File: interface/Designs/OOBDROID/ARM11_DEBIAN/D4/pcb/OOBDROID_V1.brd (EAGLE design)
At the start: 60.3 x 36.4 mm, 37 parts, among them T1 BC847, T2 BC817, U1 MCP2551, U2 MCP2551, X1 16MHz, X2 ODROID P1, X3 16MHz, X4 ODROID-P5

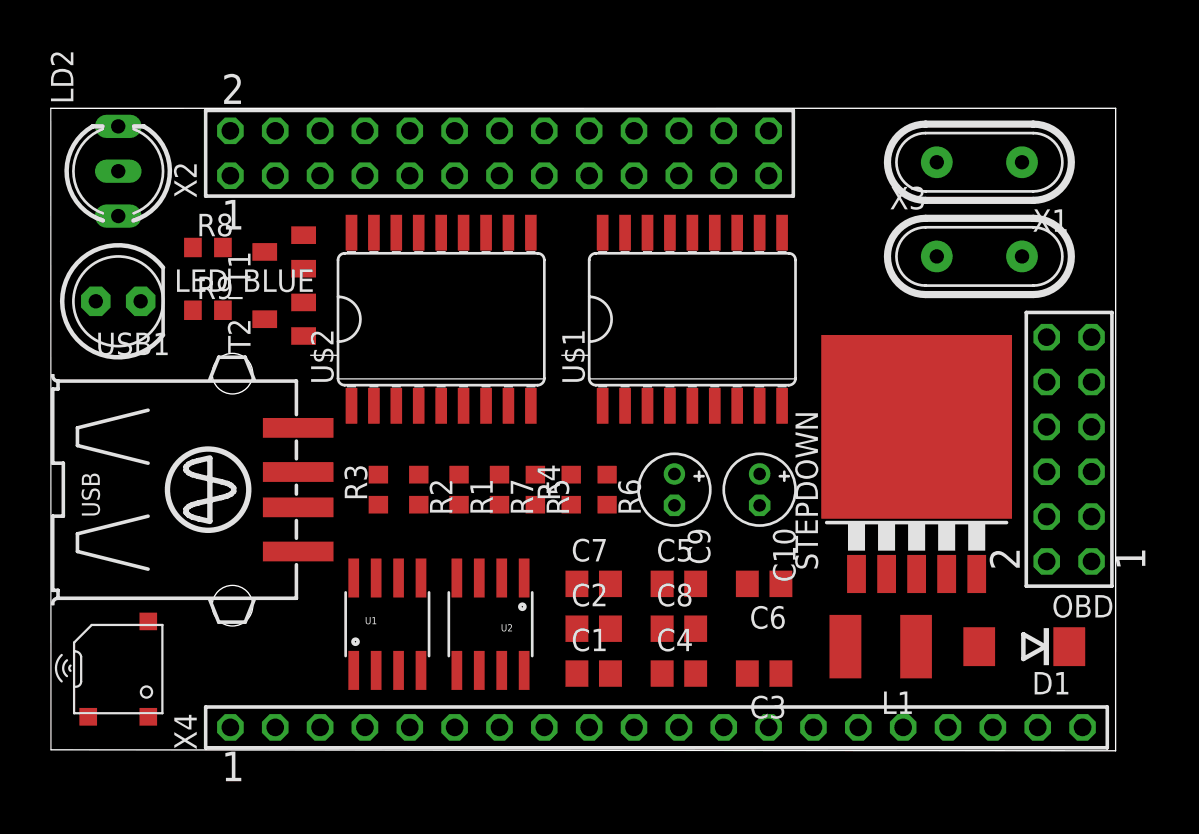
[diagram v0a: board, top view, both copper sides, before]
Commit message: add latest PCB/schematics modification for OOBDROID extension
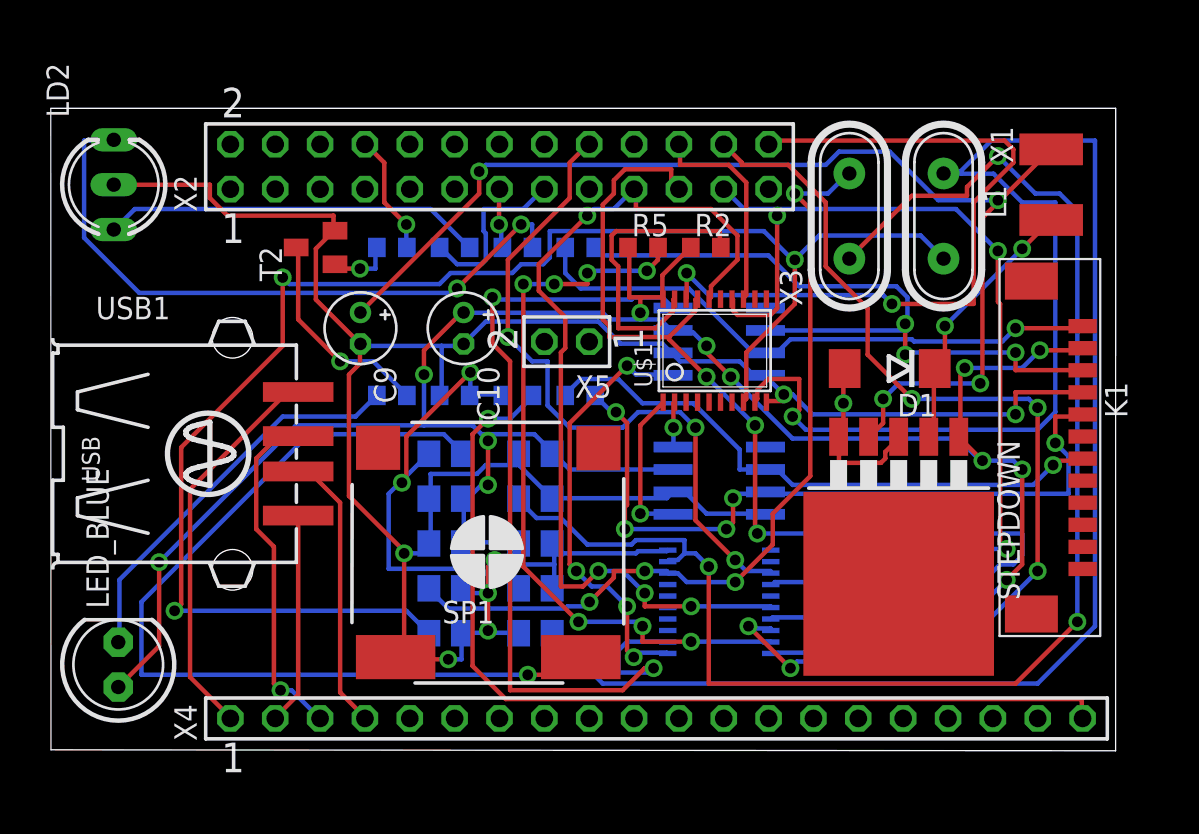
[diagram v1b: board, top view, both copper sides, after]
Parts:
- removed OBD: OOBD-CON, con-samtec:SSW-106-02-S-D
- removed R4: 4k7, eagle-ltspice:R0603
- removed SPK1: SMT-0540-S-R, adafruit:SMT-0540-S-R
- removed T1: BC847, transistor:SOT23
- added C11: 33nF, eagle-ltspice:C0805
- added C12: 10µF, eagle-ltspice:C0805
- added K1: OBD, EagleLibrary_Wuerth_Elektronik _eiCan_Wire_to_Board_Connectors_v6_20150113:653112124022
- added R12, R13: 150R, eagle-ltspice:R0603
- added SP1: LSF-15SMD, speaker:SMS-1308MS-2-R
- added X5: SSW-101-02-S-D, con-samtec:SSW-101-02-S-D
- U$1, U$2: value MCP2515SO -> MCP2515TSOP; device MCP2515_MT:SO18L -> MCP2515_MT:TSSOP20
- moved L1 27.9 mm to (56.6, 32.0), turned to 90 degrees
- moved U$2 22.5 mm to (37.8, 8.38), flipped to the bottom, turned to 90 degrees
- moved R2 21.3 mm to (37.1, 28.4), turned to 0 degrees
- moved U2 20.6 mm to (37.8, 23.1), flipped to the bottom, turned to 90 degrees
- moved LED_BLUE 20.6 mm to (3.81, 4.83), turned to 90 degrees
- moved U1 20.5 mm to (37.8, 15.2), flipped to the bottom, turned to 90 degrees
- moved C9 20.0 mm to (17.5, 23.9)
- moved C10 19.1 mm to (23.4, 23.9)
- moved R3 17.9 mm to (30.0, 28.4), flipped to the bottom, turned to 180 degrees
- moved D1 17.5 mm to (47.5, 21.6)
- moved R5 15.0 mm to (33.5, 28.4), turned to 0 degrees
- moved R6 14.6 mm to (26.4, 28.4), flipped to the bottom, turned to 180 degrees
- moved R7 13.9 mm to (22.9, 28.4), flipped to the bottom, turned to 0 degrees
- moved C4 13.4 mm to (22.4, 6.60), flipped to the bottom
- moved C5 13.4 mm to (22.4, 11.7), flipped to the bottom
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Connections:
- removed net N$20: SPK1.+, T1.3
- removed net N$21: R4.2, T1.1
- new net N$17: C12.2, SP1.M1
- new net N$37: C11.2, C12.1, R12.2, R13.2
- net GND: now also C11.1, K1.4, R13.1, SP1.M2, U$1.10, U$2.10; no longer OBD.4, T1.2, U$1.9, U$2.9
- net N$1: now also K1.5; no longer OBD.5
- net N$10: now also K1.1; no longer OBD.1
- net N$11: now also U$1.8; no longer U$1.7
- net N$12: now also U$1.9; no longer U$1.8
- net N$13: now also U$1.19; no longer U$1.17
- net N$16: now also K1.7; no longer OBD.7
- net N$19: now also U$1.18; no longer U$1.16
- net N$3: now also U$2.8; no longer U$2.7
- net N$30: now also R12.1, X4.20; no longer R4.1, X2.11
- net N$31: now also U$1.13; no longer U$1.12
- net N$32: now also U$2.13; no longer U$2.12
- net N$33: now also U$2.18; no longer U$2.16
- net N$38: now also U$1.16, U$2.16; no longer U$1.14, U$2.14
- net N$43: now also U$1.17, U$2.17; no longer U$1.15, U$2.15
- net N$44: now also U$1.14, U$2.14; no longer U$1.13, U$2.13
- net N$5: now also U$2.9; no longer U$2.8
- net N$6: now also U$2.19; no longer U$2.17
- net N$9: now also K1.3; no longer OBD.3
- net VCC: now also K1.2, U$1.20, U$2.20; no longer OBD.2, SPK1.-, U$1.18, U$2.18
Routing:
- net GND: track 0.00 -> 156.7 mm, vias 0 -> 8
- net VCC: track 0.00 -> 139.4 mm, vias 0 -> 12
- net N$12: track 0.00 -> 109.4 mm, vias 0 -> 1
- net N$11: track 0.00 -> 87.1 mm, vias 0 -> 3
- net N$5: track 0.00 -> 83.3 mm, vias 0 -> 3
- net N$43: track 0.00 -> 65.5 mm, vias 0 -> 3
- net N$4: track 0.00 -> 65.1 mm, vias 0 -> 4
- net N$33: track 0.00 -> 58.0 mm, vias 0 -> 5
- net N$44: track 0.00 -> 57.3 mm, vias 0 -> 3
- net N$30: track 0.00 -> 53.8 mm, vias 0 -> 1
- net N$17: track 0.00 -> 52.6 mm, vias 0 -> 1
- net N$38: track 0.00 -> 51.6 mm, vias 0 -> 4
- net N$7: track 0.00 -> 48.3 mm, vias 0 -> 2
- net N$3: track 0.00 -> 46.9 mm, vias 0 -> 4
- net N$19: track 0.00 -> 42.4 mm, vias 0 -> 2
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
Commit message: add latest modifcation of OOBDROID to new feature branch
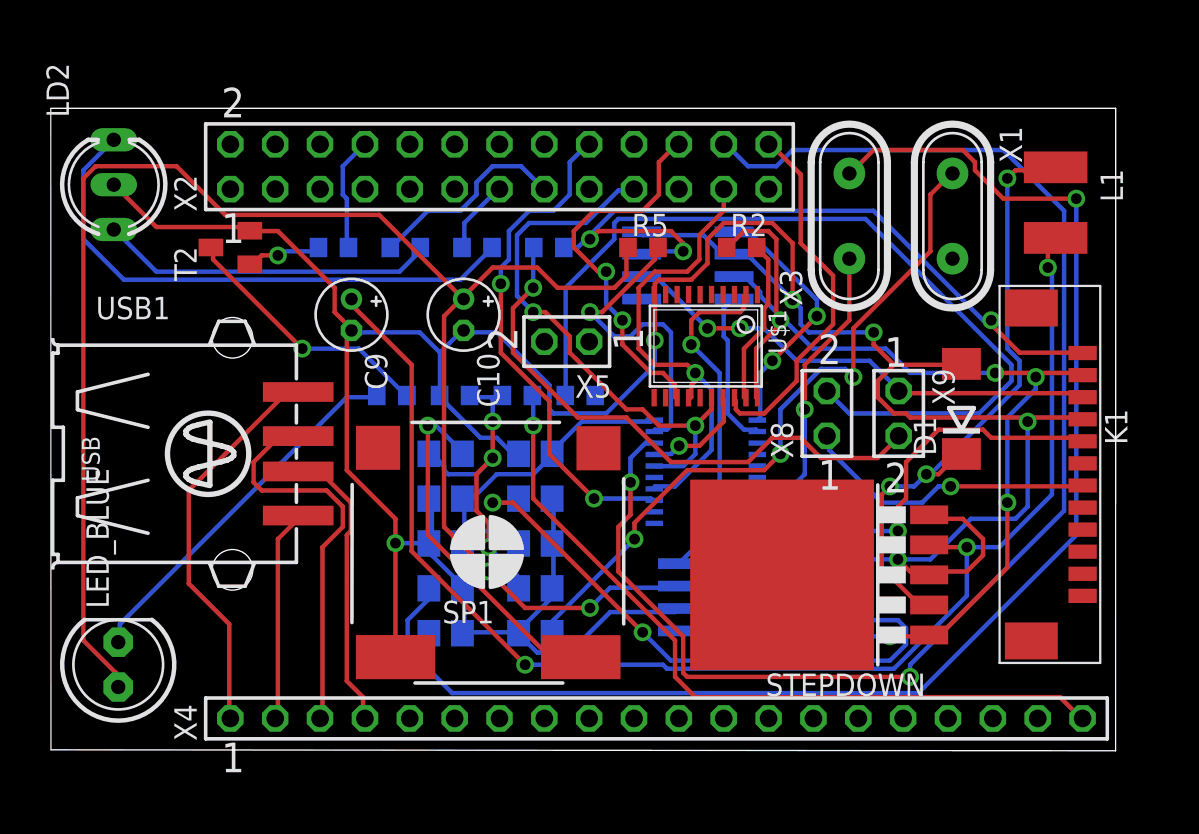
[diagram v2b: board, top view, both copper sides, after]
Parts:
- added X8, X9: TERM-DISABLE, con-samtec:SSW-101-02-S-D
- R12: value 150R -> 270R
- moved U$2 7.41 mm to (37.1, 15.7), turned to 270 degrees
- moved U1 6.61 mm to (38.1, 8.64)
- moved T2 4.83 mm to (10.2, 28.4)
- moved U2 4.67 mm to (36.1, 27.4), turned to 270 degrees
- moved D1 4.66 mm to (51.6, 19.3), turned to 90 degrees
- moved STEPDOWN 4.54 mm to (43.9, 9.91), turned to 90 degrees
- moved R8 3.30 mm to (16.0, 28.4)
- moved R7 2.79 mm to (20.1, 28.4)
- moved R6 2.29 mm to (24.1, 28.4)
- moved R2 2.03 mm to (39.1, 28.4)
- moved R3 1.78 mm to (28.2, 28.4), turned to 0 degrees
- moved K1 1.52 mm to (58.4, 21.8)
- moved L1 1.05 mm to (56.9, 31.0), turned to 270 degrees
- moved C9 0.92 mm to (17.0, 24.6)
- moved C10 0.76 mm to (23.4, 24.6)
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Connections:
- new net N$21: R3.2, X9.2
- new net N$39: R1.2, X8.2
- net N$16: now also X8.1; no longer R1.2
- net N$9: now also X9.1; no longer R3.2
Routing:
- net N$11: track 87.1 -> 0.00 mm, vias 3 -> 0
- net N$12: track 109.4 -> 39.7 mm, vias 1 -> 3
- net N$43: track 65.5 -> 6.06 mm, vias 3 -> 1
- net N$39: track 0.00 -> 49.6 mm
- net VCC: track 139.4 -> 187.7 mm, vias 12 -> 7
- net GND: track 156.7 -> 196.2 mm, vias 8 -> 6
- net N$7: track 48.3 -> 8.96 mm, vias 2 -> 0
- net N$3: track 46.9 -> 80.4 mm, vias 4 -> 1
- net N$21: track 0.00 -> 32.4 mm, vias 0 -> 1
- net N$17: track 52.6 -> 20.4 mm
- net N$44: track 57.3 -> 26.5 mm, vias 3 -> 1
- net N$6: track 41.6 -> 17.7 mm, vias 7 -> 1
- net N$33: track 58.0 -> 80.2 mm, vias 5 -> 2
- net N$19: track 42.4 -> 20.8 mm, vias 2 -> 0
- net N$38: track 51.6 -> 31.0 mm, vias 4 -> 2
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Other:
- board text added: "C1"
- board text added: "C10"
- board text added: "C11"
- board text added: "C12"
- board text added: "C2"
- board text added: "C3"
- board text added: "C4"
- board text added: "C5"
- board text added: "C6"
- board text added: "C7"
- board text added: "C8"
- board text added: "C9"
- board text added: "D1"
- board text added: "K1"
- board text added: "L1"
- board text added: "LD2"
- board text added: "LED_BLUE"
- board text added: "R1"
- board text added: "R12"
- board text added: "R13"
- board text added: "R2"
- board text added: "R3"
- board text added: "R5"
- board text added: "R6"
- board text added: "R7"
- board text added: "R8"
- board text added: "R9"
- board text added: "SP1"
- board text added: "STEPDOWN"
- board text added: "T2"
- board text added: "U$1"
- board text added: "U$2"
- board text added: "U1"
- board text added: "U2"
- board text added: "USB1"
- board text added: "X1"
- board text added: "X2"
- board text added: "X3"
- board text added: "X4"
- board text added: "X5"
- board text added: "X8"
- board text added: "X9"
